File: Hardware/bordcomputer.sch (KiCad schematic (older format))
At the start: 43 parts, among them J1 USB-B, J2 USB-A, P1 JTAG, P10 S65 Display, P11 I2C1, P12 I2C2, P13 I2C3, P14 I2C4, P2 VCC 3v3, P3 VCC 2v9, P5 VCC 5V, P6 Taster, P7 Drehencoder, P8 Tanksensor, P9 REED_FLOW, Q1 BSS123, U1 STM32F105V8, X1 8Mhz

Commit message: New Display connection + AD7843
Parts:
- removed D5: BAT54, symbol ZENER
- removed D6, D7: 6,2V, symbol DIODE
- removed L1: 820uH, symbol INDUCTOR
- removed P10: S65 Display, symbol CONN_8
- removed Q1: BSS123, symbol MOSFET_N
- removed R14: 470k, symbol R
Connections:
- net labels added: CS, IM0, IM1, IM2, IM3, RD, S65_Backlight, SD_SELECT, SPI1_MISO, SPI1_MOSI, SPI1_SCK
- net labels removed: CS (SELECT), PWM (10V), SPI1_MOSI (DATA), SPI1_SCK (CLK), VCC 2v9
- wire segments 240 -> 239
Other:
- moved on the sheet: P11, P12, P13, P14

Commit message: Modified TQFP100 pcbnew lib & first version of QSOP16 pcbnew lib
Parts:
- removed J1: USB-B, symbol USB
- removed R17: 1k5, symbol R
- added C4, C5: 0.1uF, symbol C
- added U2: AD7843, symbol AD7843
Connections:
- net labels added: ADBUSY, ADCS, JTCK, JTDI, JTDO, JTMS, NJTRST, NRST, PENIRQ, X+, X-, Y+, Y-
- net labels removed: VBUS
- wire segments 239 -> 246
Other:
- moved on the sheet: P1, R1, R2, R3

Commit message: First test version with hardware for the new MI0283QT-2 LCD
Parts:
- removed P1: JTAG, symbol CONN_10X2
- removed P12: I2C2, symbol CONN_3X2
- removed P13: I2C3, symbol CONN_3X2
- removed P14: I2C4, symbol CONN_3X2
- removed P3: VCC 2v9, symbol CONN_2
- added P14: JTAG+USART, symbol CONN_5X2
- P11: value I2C1 -> I2C
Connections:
- net labels added: LED1PWM, LED2PWM, LED3PWM, LED4PWM, USART3_RX, USART3_TX
- net labels removed: +1.8V, S65_Backlight, SD-SELECT
- wire segments 246 -> 218
- no-connect marks 3 -> 0
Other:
- moved on the sheet: C5, D2, P11, R1, R10, R2, R3

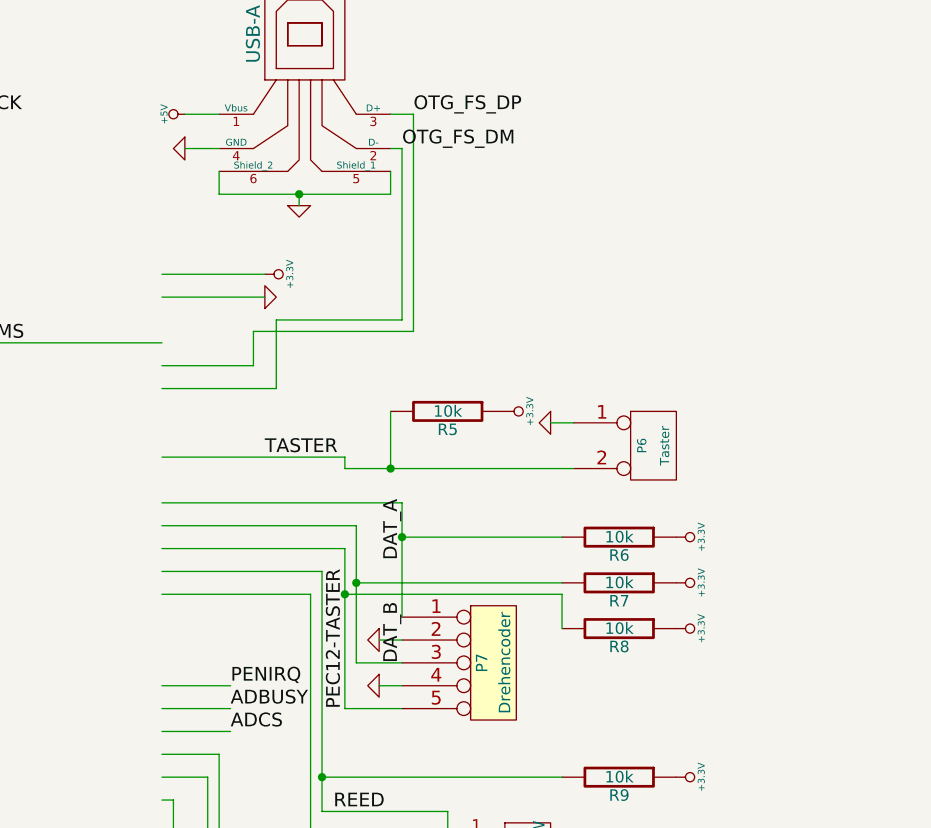
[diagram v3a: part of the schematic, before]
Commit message: added support for MI0283QT-2 display and improved main layout
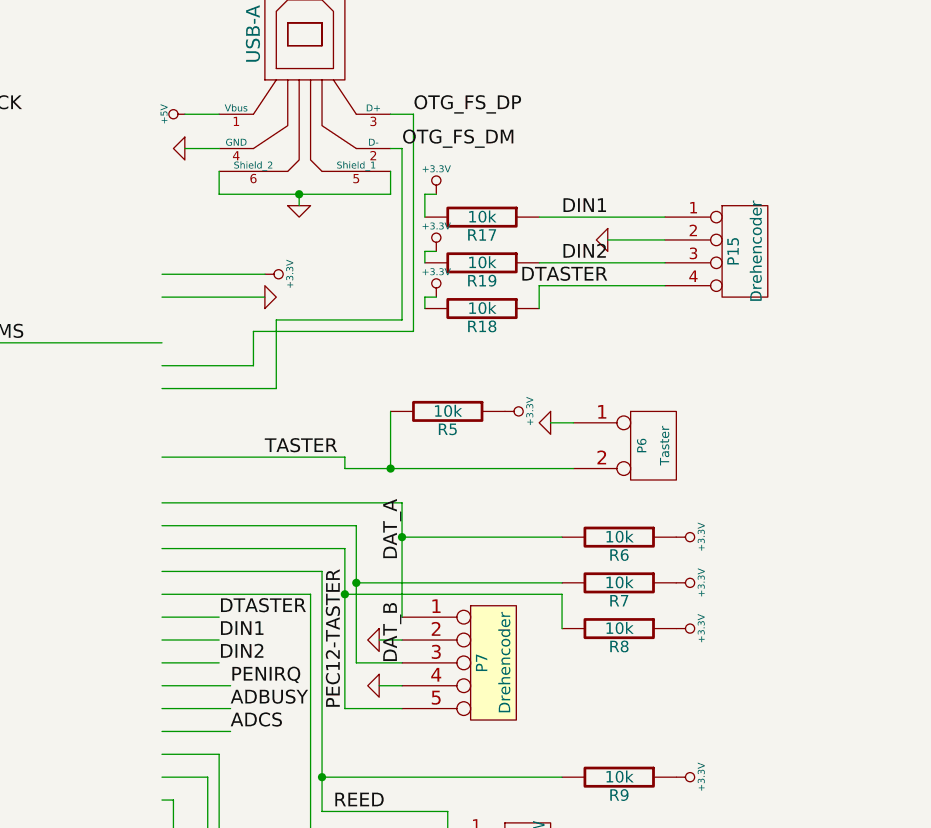
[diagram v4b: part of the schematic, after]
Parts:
- added P15: Drehencoder, symbol CONN_4
- added R17, R18, R19: 10k, symbol R
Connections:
- net labels added: DIN1, DIN2, DTASTER
- wire segments 218 -> 232

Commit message: updated display board, connection to mainboard updated
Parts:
- removed C4, C5: 0.1uF, symbol C
- removed P7: Drehencoder, symbol CONN_5
- removed R6, R7, R8: 10k, symbol R
- removed U2: AD7843, symbol AD7843
- added C?: 100nF, symbol C
- added U?: LM75CIM, symbol LM75CIM
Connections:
- net labels added: TOUCHCS
- net labels removed: DAT_A, DAT_B, PEC12-TASTER, X+, X-, Y+, Y-
- wire segments 232 -> 206
- no-connect marks 0 -> 1
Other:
- moved on the sheet: P9, R11, R9

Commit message: added capacitors to all vcc pins
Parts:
- added C10, C5, C6, C7, C8, C9: C, symbol C
- added P16: CONN_12, symbol CONN_12
- gave numbers to parts that had none: 2
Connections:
- net labels added: LCDCS, LCDLED, LCDRST, STM32_VCC1, STM32_VCC2, STM32_VCC3, STM32_VCC4, STM32_VCC5, STM32_VCCA
- net labels removed: ADCS, CS, IM0, IM1, IM2, IM3, LED1PWM, LED2PWM, LED3PWM, LED4PWM, RD, RESET, RS
- wire segments 206 -> 194

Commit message: new version schematics
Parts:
- removed BT1: BATTERY, symbol BATTERY
- removed C1, C4: 100nF, symbol C
- removed C10, C5, C6, C7, C8, C9: C, symbol C
- removed C2, C3: 22pF, symbol C
- removed D1: VCC LED, symbol LED
- removed D2: Status LED, symbol LED
- removed J2: USB-A, symbol USB
- removed P11: I2C, symbol CONN_3X2
- removed P14: JTAG+USART, symbol CONN_5X2
- removed P15: Drehencoder, symbol CONN_4
- removed P16: CONN_12, symbol CONN_12
- removed P2: VCC 3v3, symbol CONN_2
- removed P5: VCC 5V, symbol CONN_2
- removed P6: Taster, symbol CONN_2
- removed P8: Tanksensor, symbol CONN_2X2
- removed P9: REED_FLOW, symbol CONN_4
- removed R1, R11, R12, R13, R17, R18, R19, R2, R3, R5, R9: 10k, symbol R
- removed R10, R4: 22, symbol R
- removed U1: STM32F105V8, symbol STM32F10XVX
- removed U2: LM75CIM, symbol LM75CIM
- removed X1: 8Mhz, symbol CRYSTAL
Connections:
- net labels added: SPI_MISO, SPI_MOSI, SPI_SCK, UART_RX>, UART_TX<
- net labels removed: +3.3V, +5V, ADBUSY, DIN1, DIN2, DTASTER, FLOWMETER, GND, I2C2_SCL, I2C2_SDA, JTCK, JTDI, JTDO, JTMS, LCDCS, LCDLED, LCDRST, NJTRST, NRST, OTG_FS_DM, OTG_FS_DP, PENIRQ, REED, SD_SELECT, SPI1_MISO, SPI1_MOSI, SPI1_SCK, SPI2_MISO, SPI2_MOSI, SPI2_SCK, STM32_VCC1, STM32_VCC2, STM32_VCC3, STM32_VCC4, STM32_VCC5, STM32_VCCA, TASTER, TOUCHCS, USART3_RX, USART3_TX
- wire segments 194 -> 56
- no-connect marks 1 -> 0
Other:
- note added: "Analog"
